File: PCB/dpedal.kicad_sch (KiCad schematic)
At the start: 26 parts, among them J1 USB_C_Receptacle_USB2.0, J2 Conn_02x10_Counter_Clockwise, J3 Conn_ARM_JTAG_SWD_10, J4 Conn_01x05, SW1 SW_Push, SW10 SW_Push, SW2 SW_Push, SW3 SW_Push, SW4 SW_Push, SW5 RESET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

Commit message: Update symbols/footprints
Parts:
- U2: footprint Package_TO_SOT_SMD:SOT-23 -> Package_TO_SOT_SMD:SOT-23-3; symbol Regulator_Linear:MCP1703A-3302_SOT23 -> Regulator_Linear:XC6206PxxxMR
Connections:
- net 3.3V: now also U1.1 (VBAT)

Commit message: pcb fixes
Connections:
- net 3.3V: no longer U1.1 (VBAT)
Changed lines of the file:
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@@
   (junction (at 153.67 49.53) (diameter 0) (color 0 0 0 0)
-  )
-  (junction (at 127 59.69) (diameter 0) (color 0 0 0 0)
   )
   (wire (pts (xy 107.95 41.91) (xy 118.11 41.91))
@@
     (stroke (width 0) (type default))
   )
-  (wire (pts (xy 118.11 59.69) (xy 118.11 49.53))
-    (stroke (width 0) (type default))
-  )
   (wire (pts (xy 33.02 74.93) (xy 30.48 74.93))
     (stroke (width 0) (type default))
@@
     (stroke (width 0) (type default))
   )
-  (wire (pts (xy 127 63.5) (xy 129.54 63.5))
+  (wire (pts (xy 118.11 49.53) (xy 118.11 57.15))
     (stroke (width 0) (type default))
   )
@@
   )
   (wire (pts (xy 106.68 64.77) (xy 114.3 64.77))
-    (stroke (width 0) (type default))
-  )
-  (wire (pts (xy 129.54 63.5) (xy 129.54 59.69))
     (stroke (width 0) (type default))
   )
@@
     (stroke (width 0) (type default))
   )
+  (wire (pts (xy 118.11 57.15) (xy 129.54 57.15))
+    (stroke (width 0) (type default))
+  )
   (wire (pts (xy 187.96 114.3) (xy 187.96 123.19))
     (stroke (width 0) (type default))
@@
   )
   (wire (pts (xy 107.95 49.53) (xy 118.11 49.53))
-    (stroke (width 0) (type default))
-  )
-  (wire (pts (xy 127 63.5) (xy 127 59.69))
-    (stroke (width 0) (type default))
-  )
-  (wire (pts (xy 127 59.69) (xy 118.11 59.69))
     (stroke (width 0) (type default))
   )
@@
     (stroke (width 0) (type default))
   )
+  (wire (pts (xy 129.54 57.15) (xy 129.54 59.69))
+    (stroke (width 0) (type default))
+  )

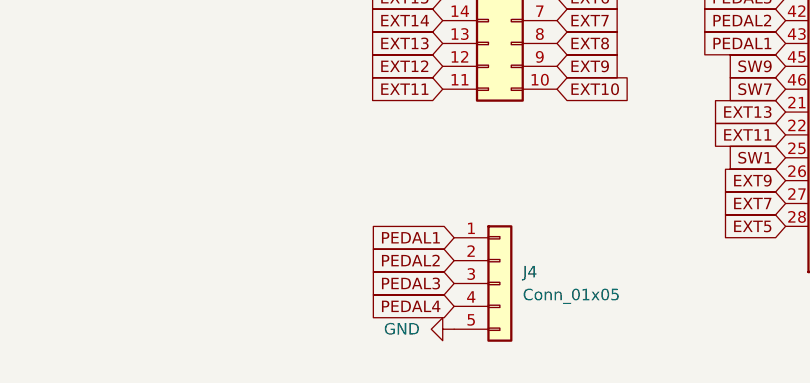
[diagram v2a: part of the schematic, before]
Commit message: PCB fix drc errors + change pedal headers to 2.54mm
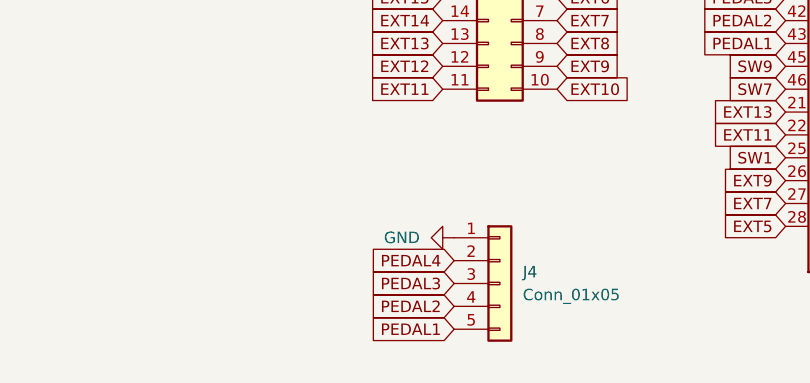
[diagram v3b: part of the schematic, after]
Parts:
- J4: footprint Connector_PinHeader_1.00mm:PinHeader_1x05_P1.00mm_Horizontal -> Connector_PinSocket_2.54mm:PinSocket_1x05_P2.54mm_Horizontal
- SW1, SW10, SW2, SW3, SW4, SW7, SW8, SW9: footprint Switch_Keyboard_Hotswap_Kailh:SW_Hotswap_Kailh_MX_plated_1.00u -> Switch_Keyboard_Hotswap_Kailh:SW_Hotswap_Kailh_MX
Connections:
- net GND: now also J4.1 (Pin_1); no longer J4.5 (Pin_5)
- net PEDAL1: now also J4.5 (Pin_5); no longer J4.1 (Pin_1)
- net PEDAL2: now also J4.4 (Pin_4); no longer J4.2 (Pin_2)
- net PEDAL4: now also J4.2 (Pin_2); no longer J4.4 (Pin_4)
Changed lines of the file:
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@@
     )
   )
-  (global_label "PEDAL2" (shape input) (at 77.47 134.62 180) (fields_autoplaced)
+  (global_label "PEDAL2" (shape input) (at 77.47 139.7 180) (fields_autoplaced)
+    (effects (font (size 1.27 1.27)) (justify right))
+    (property "Intersheetrefs" "${INTERSHEET_REFS}" (at 68.0417 139.6206 0)
+      (effects (font (size 1.27 1.27)) (justify right) hide)
+    )
+  )
+  (global_label "PEDAL4" (shape input) (at 77.47 134.62 180) (fields_autoplaced)
     (effects (font (size 1.27 1.27)) (justify right))
     (property "Intersheetrefs" "${INTERSHEET_REFS}" (at 68.0417 134.5406 0)
@@
     )
   )
-  (global_label "PEDAL4" (shape input) (at 77.47 139.7 180) (fields_autoplaced)
-    (effects (font (size 1.27 1.27)) (justify right))
-    (property "Intersheetrefs" "${INTERSHEET_REFS}" (at 68.0417 139.6206 0)
-      (effects (font (size 1.27 1.27)) (justify right) hide)
-    )
-  )
   (global_label "D-" (shape input) (at 147.32 92.71 0) (fields_autoplaced)
     (effects (font (size 1.27 1.27)) (justify left))
@@
     )
   )
-  (global_label "PEDAL1" (shape input) (at 77.47 132.08 180) (fields_autoplaced)
-    (effects (font (size 1.27 1.27)) (justify right))
-    (property "Intersheetrefs" "${INTERSHEET_REFS}" (at 68.0417 132.0006 0)
+  (global_label "PEDAL1" (shape input) (at 77.47 142.24 180) (fields_autoplaced)
+    (effects (font (size 1.27 1.27)) (justify right))
+    (property "Intersheetrefs" "${INTERSHEET_REFS}" (at 68.0417 142.1606 0)
       (effects (font (size 1.27 1.27)) (justify right) hide)
     )
@@
       (effects (font (size 1.27 1.27)))
     )
-    (property "Footprint" "Switch_Keyboard_Hotswap_Kailh:SW_Hotswap_Kailh_MX_plated_1.00u" (at 241.3 101.6 0)
+    (property "Footprint" "Switch_Keyboard_Hotswap_Kailh:SW_Hotswap_Kailh_MX" (at 241.3 101.6 0)
       (effects (font (size 1.27 1.27)) hide)
     )
@@
       (effects (font (size 1.27 1.27)))
     )
-    (property "Footprint" "Switch_Keyboard_Hotswap_Kailh:SW_Hotswap_Kailh_MX_plated_1.00u" (at 182.88 139.7 0)
+    (property "Footprint" "Switch_Keyboard_Hotswap_Kailh:SW_Hotswap_Kailh_MX" (at 182.88 139.7 0)
       (effects (font (size 1.27 1.27)) hide)
     )
@@
       (effects (font (size 1.27 1.27)))
     )
-    (property "Footprint" "Switch_Keyboard_Hotswap_Kailh:SW_Hotswap_Kailh_MX_plated_1.00u" (at 182.88 128.27 0)
+    (property "Footprint" "Switch_Keyboard_Hotswap_Kailh:SW_Hotswap_Kailh_MX" (at 182.88 128.27 0)
       (effects (font (size 1.27 1.27)) hide)
     )
@@
     )
   )
-  (symbol (lib_id "power:GND") (at 77.47 142.24 270) (unit 1)
-    (in_bom yes) (on_board yes) (dnp no) (fields_autoplaced)
-    (property "Reference" "#PWR0110" (at 71.12 142.24 0)
-      (effects (font (size 1.27 1.27)) hide)
-    )
-    (property "Value" "GND" (at 73.66 142.2399 90)
+  (symbol (lib_id "power:GND") (at 77.47 132.08 270) (unit 1)
+    (in_bom yes) (on_board yes) (dnp no)
+    (property "Reference" "#PWR0110" (at 71.12 132.08 0)
+      (effects (font (size 1.27 1.27)) hide)
+    )
+    (property "Value" "GND" (at 73.66 132.08 90)
       (effects (font (size 1.27 1.27)) (justify right))
     )
-    (property "Footprint" "" (at 77.47 142.24 0)
-      (effects (font (size 1.27 1.27)) hide)
-    )
-    (property "Datasheet" "" (at 77.47 142.24 0)
+    (property "Footprint" "" (at 77.47 132.08 0)
+      (effects (font (size 1.27 1.27)) hide)
+    )
+    (property "Datasheet" "" (at 77.47 132.08 0)
       (effects (font (size 1.27 1.27)) hide)
     )
@@
       (effects (font (size 1.27 1.27)))
     )
-    (property "Footprint" "Switch_Keyboard_Hotswap_Kailh:SW_Hotswap_Kailh_MX_plated_1.00u" (at 182.88 130.81 0)
+    (property "Footprint" "Switch_Keyboard_Hotswap_Kailh:SW_Hotswap_Kailh_MX" (at 182.88 130.81 0)
       (effects (font (size 1.27 1.27)) hide)
     )
@@
       (effects (font (size 1.27 1.27)))
     )
-    (property "Footprint" "Switch_Keyboard_Hotswap_Kailh:SW_Hotswap_Kailh_MX_plated_1.00u" (at 241.3 113.03 0)
+    (property "Footprint" "Switch_Keyboard_Hotswap_Kailh:SW_Hotswap_Kailh_MX" (at 241.3 113.03 0)
       (effects (font (size 1.27 1.27)) hide)
     )
@@
       (effects (font (size 1.27 1.27)))
     )
-    (property "Footprint" "Switch_Keyboard_Hotswap_Kailh:SW_Hotswap_Kailh_MX_plated_1.00u" (at 182.88 109.22 0)
+    (property "Footprint" "Switch_Keyboard_Hotswap_Kailh:SW_Hotswap_Kailh_MX" (at 182.88 109.22 0)
       (effects (font (size 1.27 1.27)) hide)
     )
@@
       (effects (font (size 1.27 1.27)))
     )
-    (property "Footprint" "Switch_Keyboard_Hotswap_Kailh:SW_Hotswap_Kailh_MX_plated_1.00u" (at 241.3 111.76 0)
+    (property "Footprint" "Switch_Keyboard_Hotswap_Kailh:SW_Hotswap_Kailh_MX" (at 241.3 111.76 0)
       (effects (font (size 1.27 1.27)) hide)
     )
@@
       (effects (font (size 1.27 1.27)) (justify left))
     )
-    (property "Footprint" "Connector_PinHeader_1.00mm:PinHeader_1x05_P1.00mm_Horizontal" (at 82.55 137.16 0)
+    (property "Footprint" "Connector_PinSocket_2.54mm:PinSocket_1x05_P2.54mm_Horizontal" (at 82.55 137.16 0)
       (effects (font (size 1.27 1.27)) hide)
     )
@@
       (effects (font (size 1.27 1.27)))
     )
-    (property "Footprint" "Switch_Keyboard_Hotswap_Kailh:SW_Hotswap_Kailh_MX_plated_1.00u" (at 241.3 81.28 0)
-      (effects (font (size 1.27 1.27)) hide)
-    )
+    (property "Footprint" "Switch_Keyboard_Hotswap_Kailh:SW_Hotswap_Kailh_MX" (at 241.3 81.28 0)
+      (effects (font (size 1.27 1.27)) hide)
+    )

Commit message: Finalize PCB BOM
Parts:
- J2: JLCPCB Part # (none) -> C132444
- J4: JLCPCB Part # (none) -> C124405
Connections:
- net SW4: now also U1.31 (PA10); no longer U1.30 (PA9)
- net SW8: now also U1.30 (PA9); no longer U1.31 (PA10)
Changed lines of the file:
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@@
     )
   )
-  (global_label "SW8" (shape input) (at 147.32 90.17 0) (fields_autoplaced)
-    (effects (font (size 1.27 1.27)) (justify left))
-    (property "Intersheetrefs" "${INTERSHEET_REFS}" (at 153.6036 90.2494 0)
+  (global_label "SW4" (shape input) (at 147.32 90.17 0) (fields_autoplaced)
+    (effects (font (size 1.27 1.27)) (justify left))
+    (property "Intersheetrefs" "${INTERSHEET_REFS}" (at 154.0962 90.17 0)
       (effects (font (size 1.27 1.27)) (justify left) hide)
     )
@@
     )
   )
-  (global_label "SW4" (shape input) (at 147.32 87.63 0) (fields_autoplaced)
-    (effects (font (size 1.27 1.27)) (justify left))
-    (property "Intersheetrefs" "${INTERSHEET_REFS}" (at 153.6036 87.7094 0)
+  (global_label "SW8" (shape input) (at 147.32 87.63 0) (fields_autoplaced)
+    (effects (font (size 1.27 1.27)) (justify left))
+    (property "Intersheetrefs" "${INTERSHEET_REFS}" (at 154.0962 87.63 0)
       (effects (font (size 1.27 1.27)) (justify left) hide)
     )
@@
     )
     (property "Datasheet" "~" (at 83.82 102.87 0)
+      (effects (font (size 1.27 1.27)) hide)
+    )
+    (property "JLCPCB Part #" "C132444" (at 83.82 102.87 0)
       (effects (font (size 1.27 1.27)) hide)
     )
@@
       (effects (font (size 1.27 1.27)) hide)
     )
+    (property "JLCPCB Part #" "C124405" (at 82.55 137.16 0)
+      (effects (font (size 1.27 1.27)) hide)
+    )

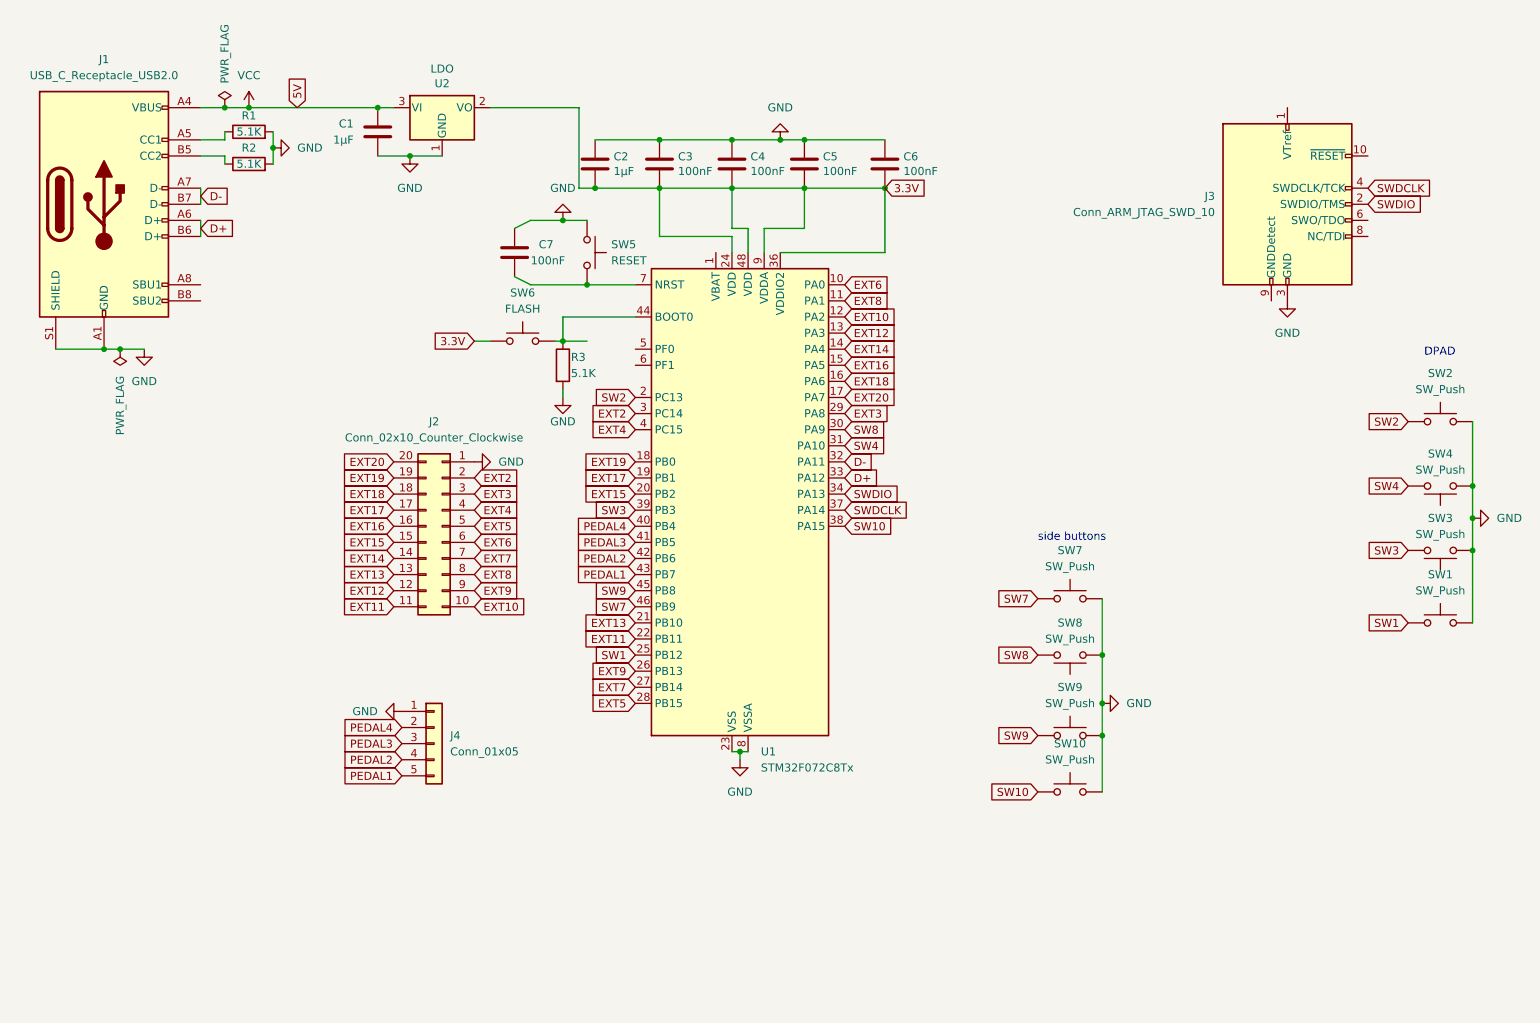
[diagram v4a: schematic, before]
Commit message: Swap out cortex debug connector for custom 2.54 pinout (2.54 will be much easier to hand solder)
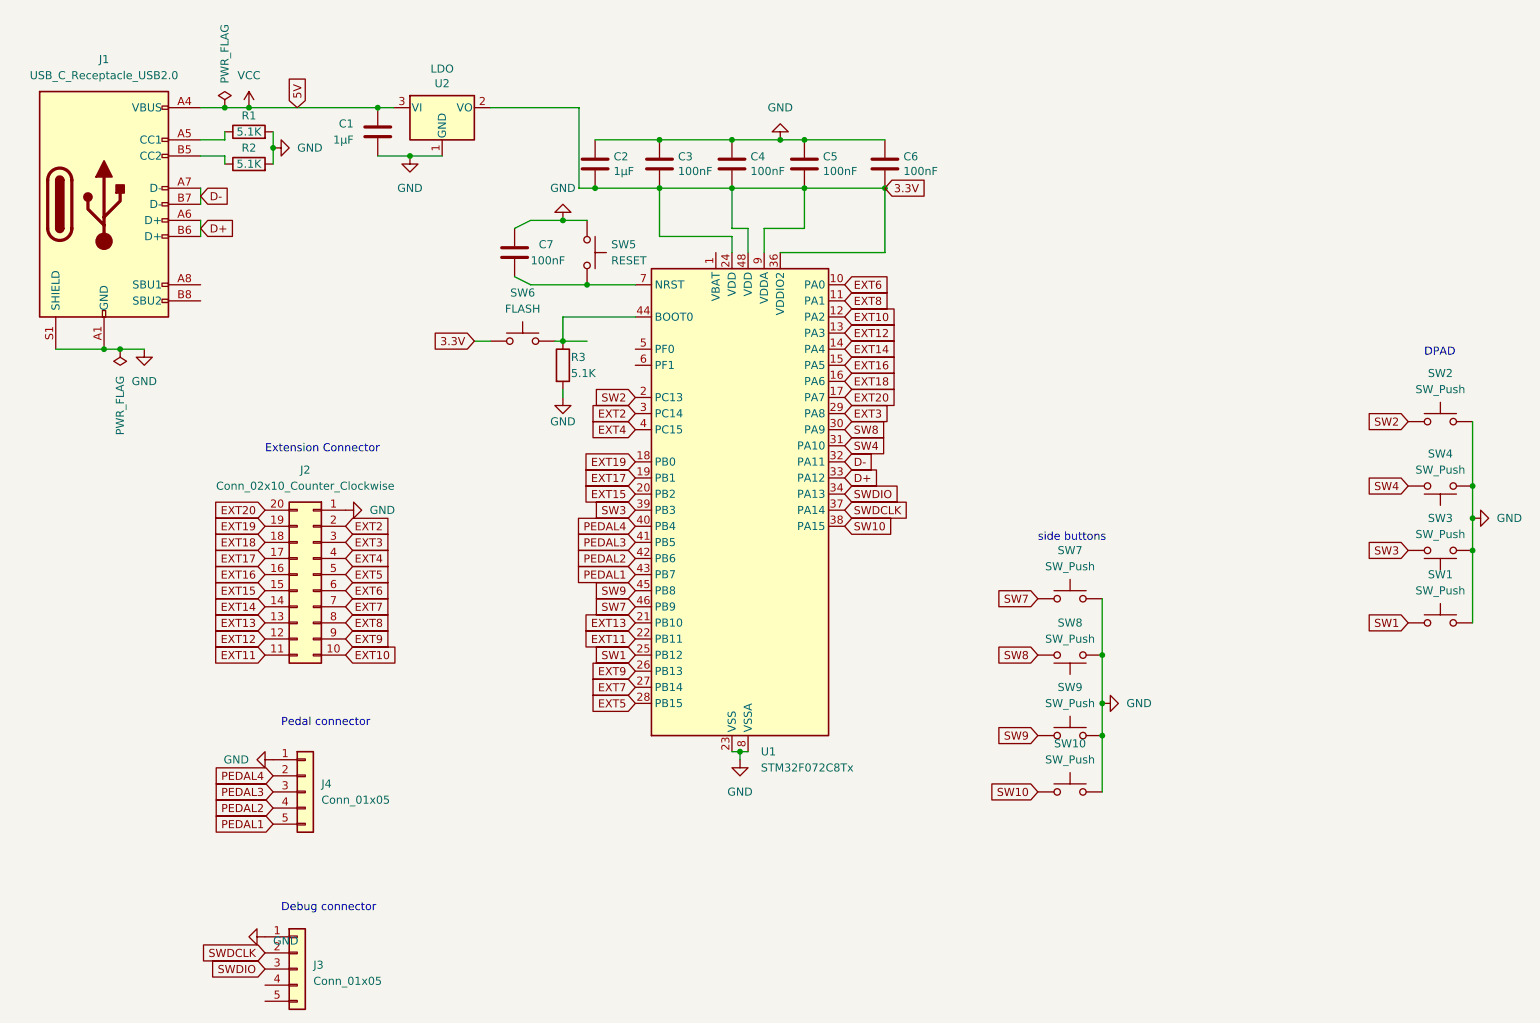
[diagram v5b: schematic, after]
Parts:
- removed J3: Conn_ARM_JTAG_SWD_10, Connector_PinHeader_1.27mm:PinHeader_2x05_P1.27mm_Vertical, symbol Connector:Conn_ARM_JTAG_SWD_10
- added J3: Conn_01x05, Connector_PinSocket_2.54mm:PinSocket_1x05_P2.54mm_Vertical, symbol Connector_Generic:Conn_01x05
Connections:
- net GND: now also J3.1 (Pin_1)
- net SWDCLK: now also J3.2 (Pin_2)
- net SWDIO: now also J3.3 (Pin_3)
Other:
- note added: "Debug connector"
- note added: "Extension Connector"
- note added: "Pedal connector"
- moved on the sheet: J2, J4
